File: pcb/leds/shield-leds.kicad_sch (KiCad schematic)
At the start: 402 parts

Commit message: [pcb][leds] starting placement
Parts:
- LED1, LED10, LED100, LED101, LED102, LED103, LED104, LED105, LED106, LED107, LED108, LED109, LED11, LED110, LED111, LED112, LED113, LED114, LED115, LED116, LED117, LED118, LED119, LED12, LED120, LED121, LED122, LED123, LED124, LED125, LED126, LED127, LED128, LED129, LED13, LED130, LED131, LED132, LED133, LED134, LED135, LED136, LED137, LED138, LED139, LED14, LED140, LED141, LED142, LED143, LED144, LED145, LED146, LED147, LED148, LED149, LED15, LED150, LED151, LED152, LED153, LED154, LED155, LED156, LED157, LED158, LED159, LED16, LED160, LED161, LED162, LED163, LED164, LED165, LED166, LED167, LED168, LED169, LED17, LED170, LED171, LED172, LED173, LED174, LED175, LED176, LED177, LED178, LED179, LED18, LED180, LED181, LED182, LED183, LED184, LED185, LED186, LED187, LED188, LED189, LED19, LED190, LED191, LED192, LED193, LED194, LED195, LED196, LED197, LED198, LED199, LED2, LED20, LED200, LED201, LED21, LED22, LED23, LED24, LED25, LED26, LED27, LED28, LED29, LED3, LED30, LED31, LED32, LED33, LED34, LED35, LED36, LED37, LED38, LED39, LED4, LED40, LED41, LED42, LED43, LED44, LED45, LED46, LED47, LED48, LED49, LED5, LED50, LED51, LED52, LED53, LED54, LED55, LED56, LED57, LED58, LED59, LED6, LED60, LED61, LED62, LED63, LED64, LED65, LED66, LED67, LED68, LED69, LED7, LED70, LED71, LED72, LED73, LED74, LED75, LED76, LED77, LED78, LED79, LED8, LED80, LED81, LED82, LED83, LED84, LED85, LED86, LED87, LED88, LED89, LED9, LED90, LED91, LED92, LED93, LED94, LED95, LED96, LED97, LED98, LED99: footprint !Misc:D_0603_1608Metric -> Diode_SMD:D_0402_1005Metric
- R1, R10, R100, R101, R102, R103, R104, R105, R106, R107, R108, R109, R11, R110, R111, R112, R113, R114, R115, R116, R117, R118, R119, R12, R120, R121, R122, R123, R124, R125, R126, R127, R128, R129, R13, R130, R131, R132, R133, R134, R135, R136, R137, R138, R139, R14, R140, R141, R142, R143, R144, R145, R146, R147, R148, R149, R15, R150, R151, R152, R153, R154, R155, R156, R157, R158, R159, R16, R160, R161, R162, R163, R164, R165, R166, R167, R168, R169, R17, R170, R171, R172, R173, R174, R175, R176, R177, R178, R179, R18, R180, R181, R182, R183, R184, R185, R186, R187, R188, R189, R19, R190, R191, R192, R193, R194, R195, R196, R197, R198, R199, R2, R20, R200, R201, R21, R22, R23, R24, R25, R26, R27, R28, R29, R3, R30, R31, R32, R33, R34, R35, R36, R37, R38, R39, R4, R40, R41, R42, R43, R44, R45, R46, R47, R48, R49, R5, R50, R51, R52, R53, R54, R55, R56, R57, R58, R59, R6, R60, R61, R62, R63, R64, R65, R66, R67, R68, R69, R7, R70, R71, R72, R73, R74, R75, R76, R77, R78, R79, R8, R80, R81, R82, R83, R84, R85, R86, R87, R88, R89, R9, R90, R91, R92, R93, R94, R95, R96, R97, R98, R99: footprint Resistor_SMD:R_0603_1608Metric -> Resistor_SMD:R_0402_1005Metric

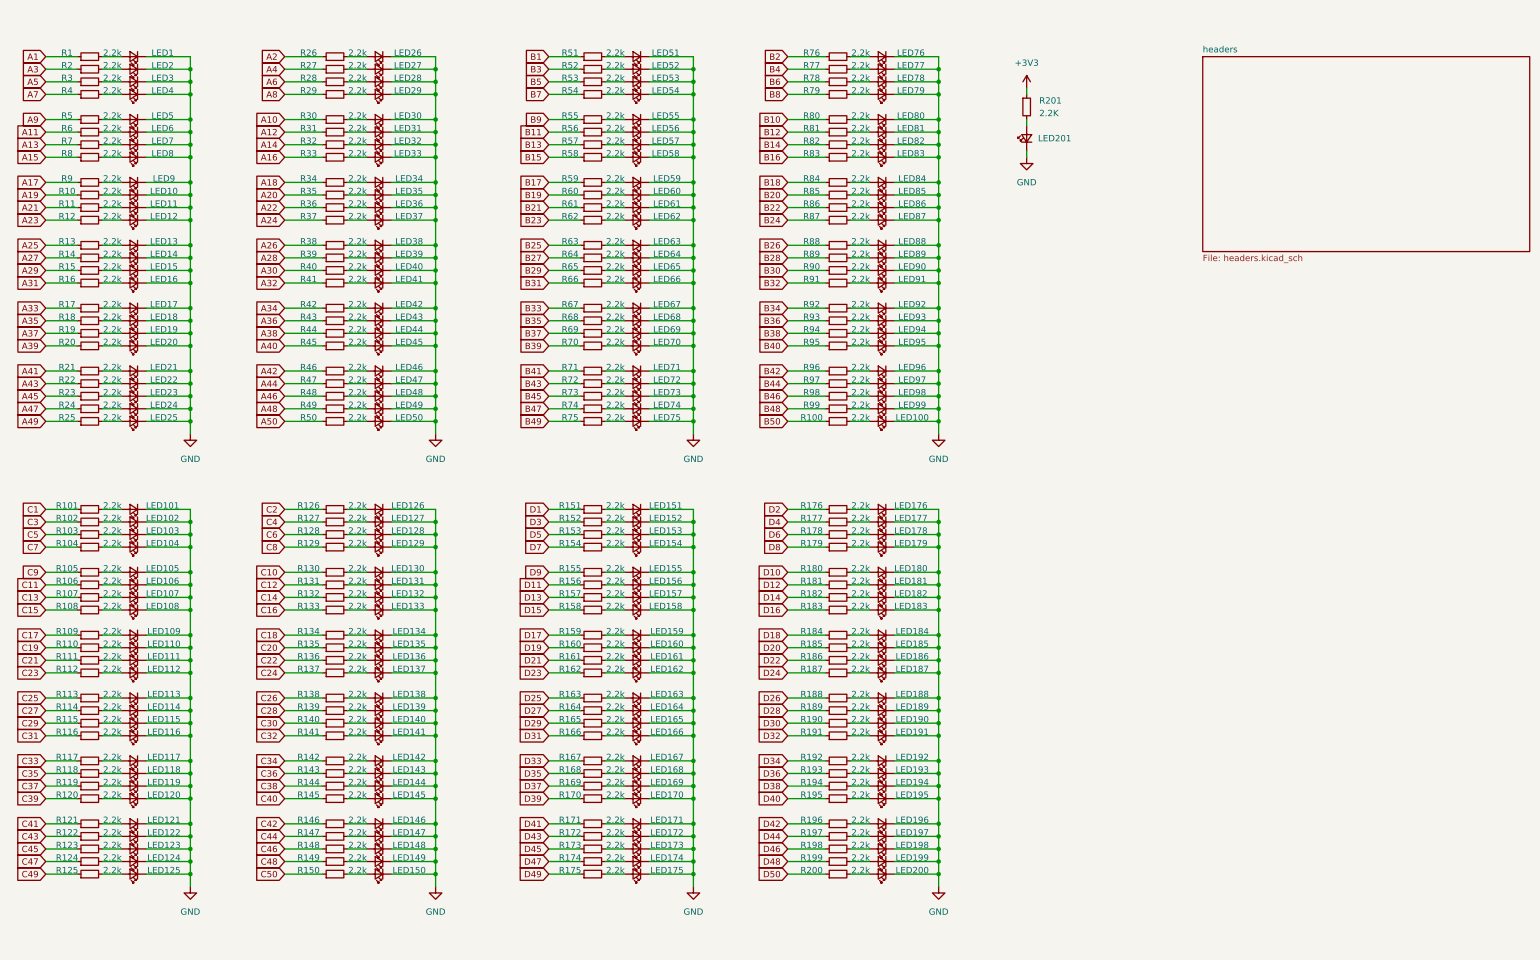
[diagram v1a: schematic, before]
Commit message: [pcb][leds] left side routed
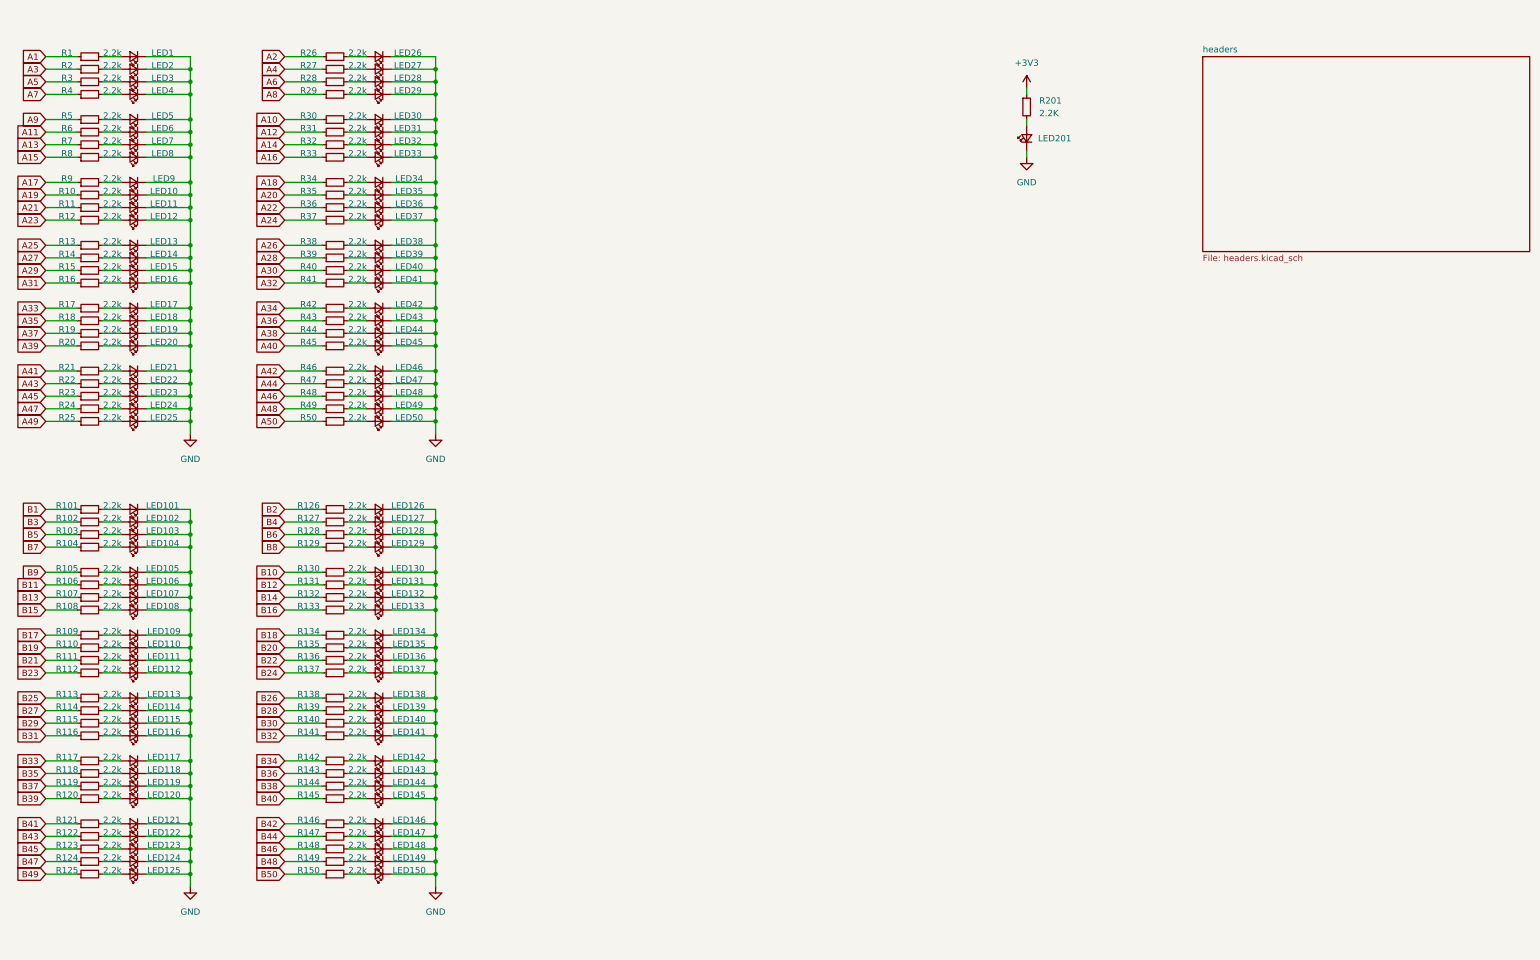
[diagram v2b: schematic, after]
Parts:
- removed LED100, LED151, LED152, LED153, LED154, LED155, LED156, LED157, LED158, LED159, LED160, LED161, LED162, LED163, LED164, LED165, LED166, LED167, LED168, LED169, LED170, LED171, LED172, LED173, LED174, LED175, LED176, LED177, LED178, LED179, LED180, LED181, LED182, LED183, LED184, LED185, LED186, LED187, LED188, LED189, LED190, LED191, LED192, LED193, LED194, LED195, LED196, LED197, LED198, LED199, LED200, LED51, LED52, LED53, LED54, LED55, LED56, LED57, LED58, LED59, LED60, LED61, LED62, LED63, LED64, LED65, LED66, LED67, LED68, LED69, LED70, LED71, LED72, LED73, LED74, LED75, LED76, LED77, LED78, LED79, LED80, LED81, LED82, LED83, LED84, LED85, LED86, LED87, LED88, LED89, LED90, LED91, LED92, LED93, LED94, LED95, LED96, LED97, LED98, LED99: Blue, Diode_SMD:D_0402_1005Metric, symbol !Misc:LED_BLU
- removed R100, R151, R152, R153, R154, R155, R156, R157, R158, R159, R160, R161, R162, R163, R164, R165, R166, R167, R168, R169, R170, R171, R172, R173, R174, R175, R176, R177, R178, R179, R180, R181, R182, R183, R184, R185, R186, R187, R188, R189, R190, R191, R192, R193, R194, R195, R196, R197, R198, R199, R200, R51, R52, R53, R54, R55, R56, R57, R58, R59, R60, R61, R62, R63, R64, R65, R66, R67, R68, R69, R70, R71, R72, R73, R74, R75, R76, R77, R78, R79, R80, R81, R82, R83, R84, R85, R86, R87, R88, R89, R90, R91, R92, R93, R94, R95, R96, R97, R98, R99: 2.2k, Resistor_SMD:R_0402_1005Metric, symbol !Misc:R_2.2K_0603
- LED1, LED10, LED101, LED102, LED103, LED104, LED105, LED106, LED107, LED108, LED109, LED11, LED110, LED111, LED112, LED113, LED114, LED115, LED116, LED117, LED118, LED119, LED12, LED120, LED121, LED122, LED123, LED124, LED125, LED126, LED127, LED128, LED129, LED13, LED130, LED131, LED132, LED133, LED134, LED135, LED136, LED137, LED138, LED139, LED14, LED140, LED141, LED142, LED143, LED144, LED145, LED146, LED147, LED148, LED149, LED15, LED150, LED16, LED17, LED18, LED19, LED2, LED20, LED21, LED22, LED23, LED24, LED25, LED26, LED27, LED28, LED29, LED3, LED30, LED31, LED32, LED33, LED34, LED35, LED36, LED37, LED38, LED39, LED4, LED40, LED41, LED42, LED43, LED44, LED45, LED46, LED47, LED48, LED49, LED5, LED50, LED6, LED7, LED8, LED9: footprint Diode_SMD:D_0402_1005Metric -> !Misc:D_0603_1608Metric
- R1, R10, R101, R102, R103, R104, R105, R106, R107, R108, R109, R11, R110, R111, R112, R113, R114, R115, R116, R117, R118, R119, R12, R120, R121, R122, R123, R124, R125, R126, R127, R128, R129, R13, R130, R131, R132, R133, R134, R135, R136, R137, R138, R139, R14, R140, R141, R142, R143, R144, R145, R146, R147, R148, R149, R15, R150, R16, R17, R18, R19, R2, R20, R21, R22, R23, R24, R25, R26, R27, R28, R29, R3, R30, R31, R32, R33, R34, R35, R36, R37, R38, R39, R4, R40, R41, R42, R43, R44, R45, R46, R47, R48, R49, R5, R50, R6, R7, R8, R9: footprint Resistor_SMD:R_0402_1005Metric -> Resistor_SMD:R_0603_1608Metric
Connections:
- net C1 is gone; now on net B1: R101.1
- net C10 is gone; now on net B10: R130.1
- net C11 is gone; now on net B11: R106.1
- net C12 is gone; now on net B12: R131.1
- net C13 is gone; now on net B13: R107.1
- net C14 is gone; now on net B14: R132.1
- net C15 is gone; now on net B15: R108.1
- net C16 is gone; now on net B16: R133.1
- net C17 is gone; now on net B17: R109.1
- net C18 is gone; now on net B18: R134.1
- net C19 is gone; now on net B19: R110.1
- net C2 is gone; now on net B2: R126.1
- net C20 is gone; now on net B20: R135.1
- net C21 is gone; now on net B21: R111.1
- net C22 is gone; now on net B22: R136.1
- net C23 is gone; now on net B23: R112.1
- net C24 is gone; now on net B24: R137.1
- net C25 is gone; now on net B25: R113.1
- net C26 is gone; now on net B26: R138.1
- net C27 is gone; now on net B27: R114.1
- net C28 is gone; now on net B28: R139.1
- net C29 is gone; now on net B29: R115.1
- net C3 is gone; now on net B3: R102.1
- net C30 is gone; now on net B30: R140.1
- net C31 is gone; now on net B31: R116.1
- net C32 is gone; now on net B32: R141.1
- net C33 is gone; now on net B33: R117.1
- net C34 is gone; now on net B34: R142.1
- net C35 is gone; now on net B35: R118.1
- net C36 is gone; now on net B36: R143.1
- net C37 is gone; now on net B37: R119.1
- net C38 is gone; now on net B38: R144.1
- net C39 is gone; now on net B39: R120.1
- net C4 is gone; now on net B4: R127.1
- net C40 is gone; now on net B40: R145.1
- net C41 is gone; now on net B41: R121.1
- net C42 is gone; now on net B42: R146.1
- net C43 is gone; now on net B43: R122.1
- net C44 is gone; now on net B44: R147.1
- net C45 is gone; now on net B45: R123.1
- net C46 is gone; now on net B46: R148.1
- net C47 is gone; now on net B47: R124.1
- net C48 is gone; now on net B48: R149.1
- net C49 is gone; now on net B49: R125.1
- net C5 is gone; now on net B5: R103.1
- net C50 is gone; now on net B50: R150.1
- net C6 is gone; now on net B6: R128.1
- net C7 is gone; now on net B7: R104.1
- net C8 is gone; now on net B8: R129.1
- net C9 is gone; now on net B9: R105.1

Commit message: [pcb][leds] fully routed
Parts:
- added J1: QTH-060-01-L-D-A, !Misc:SAMTEC_QTH-060-01-X-D-A, symbol !Misc:QTH-060-01-L-D-A
- LED201: footprint Diode_SMD:D_0402_1005Metric -> !Misc:D_0603_1608Metric
- R201: footprint Resistor_SMD:R_0402_1005Metric -> Resistor_SMD:R_0603_1608Metric
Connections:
- net +3V3: now also J1.10, J1.101, J1.102, J1.111, J1.112, J1.19, J1.20, J1.29, J1.30, J1.39, J1.40, J1.49, J1.50, J1.71, J1.72, J1.81, J1.82, J1.9, J1.91, J1.92
- net A1: now also J1.1
- net A10: now also J1.12
- net A11: now also J1.13
- net A12: now also J1.14
- net A13: now also J1.15
- net A14: now also J1.16
- net A15: now also J1.17
- net A16: now also J1.18
- net A17: now also J1.21
- net A18: now also J1.22
- net A19: now also J1.23
- net A2: now also J1.2
- net A20: now also J1.24
- net A21: now also J1.25
- net A22: now also J1.26
- net A23: now also J1.27
- net A24: now also J1.28
- net A25: now also J1.31
- net A26: now also J1.32
- net A27: now also J1.33
- net A28: now also J1.34
- net A29: now also J1.35
- net A3: now also J1.3
- net A30: now also J1.36
- net A31: now also J1.37
- net A32: now also J1.38
- net A33: now also J1.41
- net A34: now also J1.42
- net A35: now also J1.43
- net A36: now also J1.44
- net A37: now also J1.45
- net A38: now also J1.46
- net A39: now also J1.47
- net A4: now also J1.4
- net A40: now also J1.48
- net A41: now also J1.51
- net A42: now also J1.52
- net A43: now also J1.53
- net A44: now also J1.54
- net A45: now also J1.55
- net A46: now also J1.56
- net A47: now also J1.57
- net A48: now also J1.58
- net A49: now also J1.59
- net A5: now also J1.5
- net A50: now also J1.60
- net A6: now also J1.6
- net A7: now also J1.7
- net A8: now also J1.8
- net A9: now also J1.11
- net B1: now also J1.61
- net B10: now also J1.70
- net B11: now also J1.73
- net B12: now also J1.74
- net B13: now also J1.75
- net B14: now also J1.76
- net B15: now also J1.77
- net B16: now also J1.78
- net B17: now also J1.79
- net B18: now also J1.80
- net B19: now also J1.83
- net B2: now also J1.62
- net B20: now also J1.84
- net B21: now also J1.85
- net B22: now also J1.86
- net B23: now also J1.87
- net B24: now also J1.88
- net B25: now also J1.89
- net B26: now also J1.90
- net B27: now also J1.93
- net B28: now also J1.94
- net B29: now also J1.95
- net B3: now also J1.63
- net B30: now also J1.96
- net B31: now also J1.97
- net B32: now also J1.98
- net B33: now also J1.99
- net B34: now also J1.100
- net B35: now also J1.103
- net B36: now also J1.104
- net B37: now also J1.105
- net B38: now also J1.106
- net B39: now also J1.107
- net B4: now also J1.64
- net B40: now also J1.108
- net B41: now also J1.109
- net B42: now also J1.110
- net B43: now also J1.113
- net B44: now also J1.114
- net B45: now also J1.115
- net B46: now also J1.116
- net B47: now also J1.117
- net B48: now also J1.118
- net B49: now also J1.119
- net B5: now also J1.65
- net B50: now also J1.120
- net B6: now also J1.66
- net B7: now also J1.67
- net B8: now also J1.68
- net B9: now also J1.69
- net GND: now also J1.GND
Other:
- removed sheet headers
- moved on the sheet: LED1, LED10, LED101, LED102, LED103, LED104, LED105, LED106, LED107, LED108, LED109, LED11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

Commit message: [pcb] misc fixes during jlcpcb production submission
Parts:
- R1, R10, R101, R102, R103, R104, R105, R106, R107, R108, R109, R11, R110, R111, R112, R113, R114, R115, R116, R117, R118, R119, R12, R120, R121, R122, R123, R124, R125, R126, R127, R128, R129, R13, R130, R131, R132, R133, R134, R135, R136, R137, R138, R139, R14, R140, R141, R142, R143, R144, R145, R146, R147, R148, R149, R15, R150, R16, R17, R18, R19, R2, R20, R201, R21, R22, R23, R24, R25, R26, R27, R28, R29, R3, R30, R31, R32, R33, R34, R35, R36, R37, R38, R39, R4, R40, R41, R42, R43, R44, R45, R46, R47, R48, R49, R5, R50, R6, R7, R8, R9: LCSC Part # C25879 -> C4190
